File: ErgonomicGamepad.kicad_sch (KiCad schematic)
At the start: 84 parts, among them J1 USB_C_Receptacle_USB2.0_16P, J2 Conn_01x05, J3 Conn_01x05, J4 Conn_01x05, J5 AVR-ISP-6, J6 Conn_01x05, J7 1824417, SW01 SW_DIP_x01, SW02 SW_DIP_x01, SW03 SW_DIP_x01, SW04 SW_DIP_x01, SW05 SW_DIP_x01, SW06 SW_DIP_x01, SW07 SW_DIP_x01, SW08 SW_DIP_x01, SW09 SW_DIP_x01, SW10 SW_DIP_x01, SW11 SW_DIP_x01, SW12 SW_DIP_x01, SW13 SW_DIP_x01, SW14 SW_DIP_x01, SW15 SW_DIP_x01, SW16 SW_DIP_x01, SW17 SW_DIP_x01, SW18 SW_DIP_x01, SW19 SW_DIP_x01, SW20 SW_DIP_x01, SW21 SW_DIP_x01, SW22 SW_DIP_x01, SW23 SW_DIP_x01, SW24 SW_DIP_x01, U1 ATmega32U4-A, U2 USBLC6-2SC6, Y1 Crystal

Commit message: Fill JST connector sourcing fields, refresh production reports, and lock USB-C decisions
- J2/J3/J4/J6: fill Manufacturer/MPN/Supplier/LCSC (JST B5B-XH-A(LF)(SN), C157991)
- Regenerate jlc_sourcing_bom_template.csv from current schematic state
- Rename jlc_stock_check_queue.csv -> verify_stock_before_ordering.csv and
  repurpose it as a pre-order stock/sourcing risk checklist now that all
  parts carry LCSC numbers
- Remove stale current_sch_fields.csv scratch export
- Regenerate erc-report.rpt and drc-report.rpt against current schematic/PCB
- Document resolved USB-C implementation (reversible orientation, CC
  pulldowns, ESD array, shield grounding, power-path gating) in README
- Update PROCESS.md checklist to reflect completed sourcing and USB-C
  requirements-freeze items
- Remove stray untracked-from-disk files (M1.kicad_sch, "Original
  ErgonomicGamepad.kicad_sch", "Was ErgonomicGamepad.kicad_sch", "checked
  PROCESS.md")
- Include in-progress PCB footprint placement updates

Co-Authored-By: Claude Sonnet 5 <noreply@anthropic.com>
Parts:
- J2, J3, J4, J6: LCSC (none) -> C157991; MPN (none) -> B5B-XH-A(LF)(SN); Manufacturer (none) -> JST; Supplier (none) -> LCSC
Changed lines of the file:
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@@
 			)
 		)
+		(property "Manufacturer" "JST"
+			(at 39.37 146.05 0)
+			(hide yes)
+			(show_name no)
+			(do_not_autoplace no)
+			(effects
+				(font
+					(size 1.27 1.27)
+				)
+			)
+		)
+		(property "MPN" "B5B-XH-A(LF)(SN)"
+			(at 39.37 146.05 0)
+			(hide yes)
+			(show_name no)
+			(do_not_autoplace no)
+			(effects
+				(font
+					(size 1.27 1.27)
+				)
+			)
+		)
+		(property "Supplier" "LCSC"
+			(at 39.37 146.05 0)
+			(hide yes)
+			(show_name no)
+			(do_not_autoplace no)
+			(effects
+				(font
+					(size 1.27 1.27)
+				)
+			)
+		)
+		(property "LCSC" "C157991"
+			(at 39.37 146.05 0)
+			(hide yes)
+			(show_name no)
+			(do_not_autoplace no)
+			(effects
+				(font
+					(size 1.27 1.27)
+				)
+			)
+		)
 		(pin "5"
 		)
@@
 			)
 		)
+		(property "Manufacturer" "JST"
+			(at 59.69 146.05 0)
+			(hide yes)
+			(show_name no)
+			(do_not_autoplace no)
+			(effects
+				(font
+					(size 1.27 1.27)
+				)
+			)
+		)
+		(property "MPN" "B5B-XH-A(LF)(SN)"
+			(at 59.69 146.05 0)
+			(hide yes)
+			(show_name no)
+			(do_not_autoplace no)
+			(effects
+				(font
+					(size 1.27 1.27)
+				)
+			)
+		)
+		(property "Supplier" "LCSC"
+			(at 59.69 146.05 0)
+			(hide yes)
+			(show_name no)
+			(do_not_autoplace no)
+			(effects
+				(font
+					(size 1.27 1.27)
+				)
+			)
+		)
+		(property "LCSC" "C157991"
+			(at 59.69 146.05 0)
+			(hide yes)
+			(show_name no)
+			(do_not_autoplace no)
+			(effects
+				(font
+					(size 1.27 1.27)
+				)
+			)
+		)
 		(pin "5"
 		)
@@
 			)
 		)
+		(property "Manufacturer" "JST"
+			(at 39.37 176.53 0)
+			(hide yes)
+			(show_name no)
+			(do_not_autoplace no)
+			(effects
+				(font
+					(size 1.27 1.27)
+				)
+			)
+		)
+		(property "MPN" "B5B-XH-A(LF)(SN)"
+			(at 39.37 176.53 0)
+			(hide yes)
+			(show_name no)
+			(do_not_autoplace no)
+			(effects
+				(font
+					(size 1.27 1.27)
+				)
+			)
+		)
+		(property "Supplier" "LCSC"
+			(at 39.37 176.53 0)
+			(hide yes)
+			(show_name no)
+			(do_not_autoplace no)
+			(effects
+				(font
+					(size 1.27 1.27)
+				)
+			)
+		)
+		(property "LCSC" "C157991"
+			(at 39.37 176.53 0)
+			(hide yes)
+			(show_name no)
+			(do_not_autoplace no)
+			(effects
+				(font
+					(size 1.27 1.27)
+				)
+			)
+		)
 		(pin "5"
 		)
@@
 			(at 59.69 176.53 0)
 			(hide yes)
+			(show_name no)
+			(do_not_autoplace no)
+			(effects
+				(font
+					(size 1.27 1.27)
+				)
+			)
+		)
+		(property "Manufacturer" "JST"
+			(at 59.69 176.53 0)
+			(hide yes)
+			(show_name no)
+			(do_not_autoplace no)
+			(effects
+				(font
+					(size 1.27 1.27)
+				)
+			)
+		)
+		(property "MPN" "B5B-XH-A(LF)(SN)"
+			(at 59.69 176.53 0)
+			(hide yes)
+			(show_name no)
+			(do_not_autoplace no)
+			(effects
+				(font
+					(size 1.27 1.27)
+				)
+			)
+		)
+		(property "Supplier" "LCSC"
+			(at 59.69 176.53 0)
+			(hide yes)
+			(show_name no)
+			(do_not_autoplace no)
+			(effects
+				(font
+					(size 1.27 1.27)
+				)
+			)
+		)
+		(property "LCSC" "C157991"
+			(at 59.69 176.53 0)
+			(hide yes)

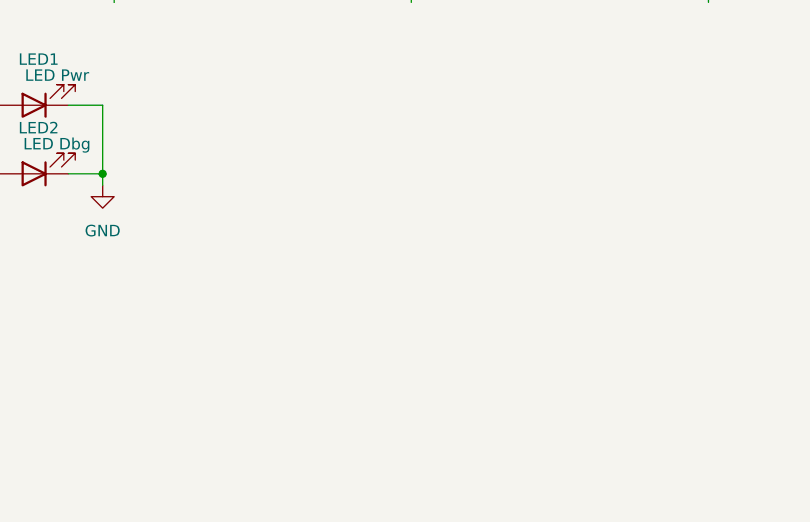
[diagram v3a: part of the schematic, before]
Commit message: Add TP8/TP9 power-rail test points, group keys, and arrange all 24 on a 20mm grid
- Add TP8 (+5V) / TP9 (GND) edge-mounted clip test points via schematic +
  Update PCB from Schematic, using a 3mm THT pad footprint suited to
  alligator/hook clips (distinct from TP1-7's fine-probe pads); document
  the split in README
- Establish SW01/DM01 as the validated "key" placement template: diode
  clear of the socket courtyard, correct cathode-to-column orientation,
  connecting trace routed, silkscreen labels matching the rest of the board
- Add 03_apply_key_template.py to replicate that template's relative
  offset/rotation/trace onto SW02-24/DM02-24, including a fix for pads that
  carry their own explicit rotation (previously left stale, misaligning
  copper relative to the rotated body)
- Add 04_group_keys.py to group each SW0N/DM0N pair with its connecting
  trace into a named KeyNN group, matching the existing Key01 grouping
- Add 05_grid_keys.py to arrange all 24 keys on a uniform grid (default
  20mm pitch), rebuilding each key's diode position/rotation and trace
  from the template, and updating each KeyNN group's members to match;
  fixes an off-by-one in segment deletion and a missing-space bug in the
  group-members rewrite, found via DRC/paren-balance verification after
  the first run corrupted the file
- Renumber scripts/ with 01-05 prefixes reflecting invention/workflow order
- Regenerate erc-report.rpt and drc-report.rpt against the final state

Co-Authored-By: Claude Sonnet 5 <noreply@anthropic.com>
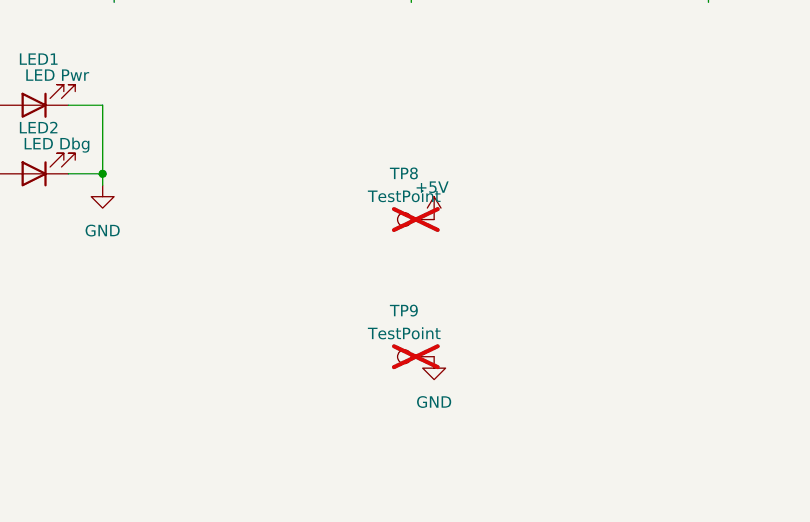
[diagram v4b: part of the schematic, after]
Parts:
- added TP8, TP9: TestPoint, TestPoint:TestPoint_THTPad_D3.0mm_Drill1.5mm, symbol Connector:TestPoint
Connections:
- net +5V: now also TP8.1
- net GND: now also TP9.1
